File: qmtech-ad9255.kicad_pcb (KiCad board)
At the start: 4 copper layers, 70 x 90 mm, 78 parts

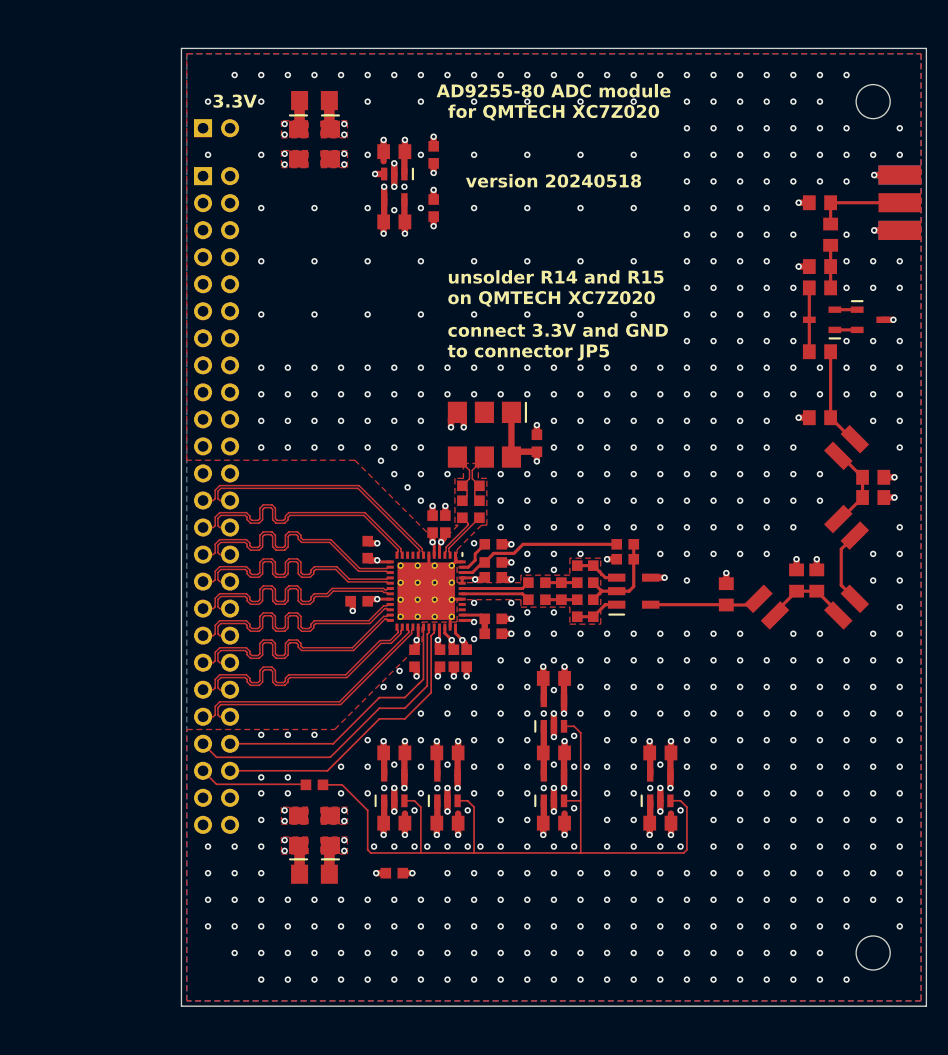
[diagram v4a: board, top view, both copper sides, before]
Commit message: replace TPS7A20 with TLV1117LV in qmtech-ad9255
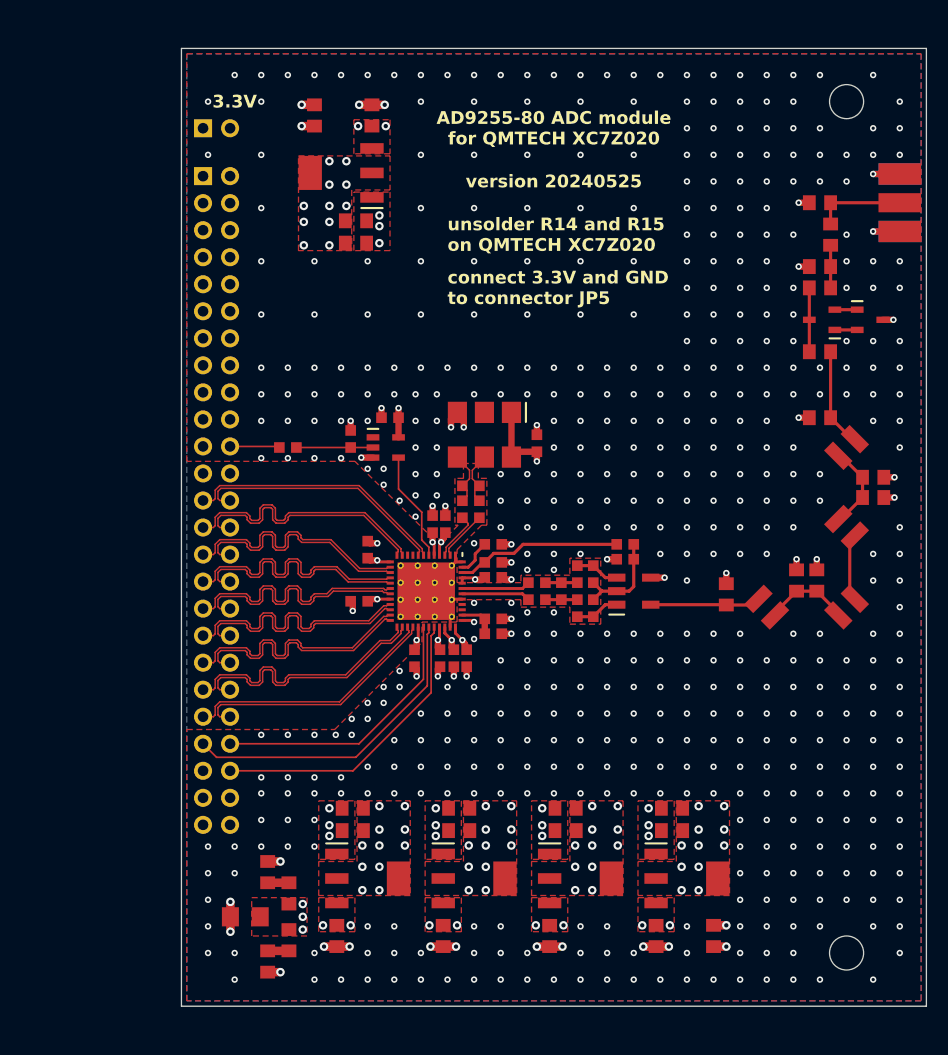
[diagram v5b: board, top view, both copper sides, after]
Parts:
- removed C31, C32: , footprints:CASE-A-3216
- removed FB2: , footprints:1206
- added R14: , footprints:0805, F.Cu at (175.0, 130.9)
- added R15: , footprints:0805, F.Cu at (141.1, 118.9)
- added R16: , footprints:0805, F.Cu at (151.1, 118.9)
- added R17: , footprints:0805, F.Cu at (161.1, 118.9)
- added R18: , footprints:0805, F.Cu at (171.1, 118.9)
- added R19: , footprints:0805, F.Cu at (137.5, 53.8)
- added R20: , footprints:0805, F.Cu at (141.4, 65.8)
- C29: footprint footprints:CASE-A-3216 -> footprints:0805
- C30: footprint footprints:CASE-A-3216 -> footprints:0603
- IC2, IC3, IC4, IC5, IC6: footprint footprints:SOT23-5 -> footprints:SOT223-3
- R12, R13: footprint footprints:0603 -> footprints:0805
- moved R12 72.5 mm to (133.1, 133.3), turned to -90 degrees
- moved C28 68.2 mm to (135.1, 131.3), turned to -90 degrees
- moved C26 55.6 mm to (142.9, 53.8), turned to 90 degrees
- moved IC6 54.6 mm to (140.0, 59.2), turned to 0 degrees
- moved C30 39.2 mm to (144.6, 82.2), turned to 180 degrees
- moved C18 32.2 mm to (139.6, 130.9), turned to -90 degrees
- moved R10 31.8 mm to (135.0, 85.0)
- moved C19 29.8 mm to (141.1, 121.0), turned to 180 degrees
- moved IC2 28.8 mm to (142.5, 125.5), turned to 180 degrees
- moved R11 27.8 mm to (140.9, 84.2), turned to 90 degrees
- moved IC7 24.5 mm to (144.2, 85.0), turned to 180 degrees
- moved IC4 15.1 mm to (162.5, 125.5), turned to 180 degrees
- moved IC5 15.1 mm to (172.5, 125.5), turned to 180 degrees
- moved C22 14.3 mm to (159.6, 130.9), turned to -90 degrees
- moved C24 14.3 mm to (169.6, 130.9), turned to -90 degrees
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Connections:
- C19 pad 1: CVDD -> DVDD
- C21 pad 1: DVDD -> SVDD
- C23 pad 1: SVDD -> AVDD
- C25 pad 1: 3V -> CVDD
- C26 pad 1: AVDD -> VIN2
- C27 pad 1: VCCO33 -> VCCO25
- C28 pad 1: VCCO25 -> 5V
- C28 pad 2: GND -> DMP1
- C29 pad 1: VIN1 -> 5V
- C29 pad 2: GND -> DMP2
- C30 pad 1: 5V -> DVDD
- CN2 pad 22: (no net) -> IN1
- CN2 pad 45: IN1 -> (no net)
- IC1 pad 6: GND -> OE2
- IC2 pad 1: 5V -> GND
- IC2 pad 2: GND -> DVDD
- IC2 pad 3: AEN -> 5V
- IC3 pad 1: 5V -> GND
- IC3 pad 2: GND -> SVDD
- IC3 pad 3: AEN -> 5V
- IC4 pad 1: 5V -> GND
- IC4 pad 2: GND -> AVDD
- IC4 pad 3: AEN -> 5V
- IC5 pad 1: 5V -> GND
- IC5 pad 2: GND -> CVDD
- IC5 pad 3: AEN -> 5V
- IC6 pad 1: 3V -> GND
- IC6 pad 2: GND -> VCCO25
- IC6 pad 3: AEN -> VIN2
- IC7 pad 1: VCCO33 -> (no net)
- IC7 pad 2: GND -> OE1
- IC7 pad 3: VCCO33 -> GND
- IC7 pad 4: GND -> OE2
- IC7 pad 5: VCCO25 -> DVDD
- R10 pad 2: AEN -> OE1
- R11 pad 1: VCCO33 -> OE1
- R12 pad 1: VCCO25 -> DMP1
- R13 pad 1: 5V -> DMP2
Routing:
- net AEN: track 71.8 -> 0.00 mm
- net GND: track 97.4 -> 62.3 mm, vias 658 -> 585
- net 5V: track 16.5 -> 1.20 mm, vias 7 -> 12
- net OE2: track 0.00 -> 10.4 mm
- net VCCO33: track 7.71 -> 0.00 mm, vias 5 -> 0
- net OE1: track 0.00 -> 7.20 mm
- net IN1: track 10.2 -> 4.67 mm
- net 3V: track 4.64 -> 0.00 mm
- net VCCO25: track 4.12 -> 0.00 mm, vias 2 -> 11
- net SVDD: track 5.57 -> 2.35 mm, vias 2 -> 12
- net CVDD: track 10.9 -> 7.70 mm, vias 2 -> 12
- net AVDD: track 15.7 -> 12.4 mm, vias 6 -> 16
- net DMP2: track 0.00 -> 2.00 mm
- net DMP1: track 0.00 -> 2.00 mm
- net VIN2: track 2.74 -> 1.20 mm, vias 2 -> 3
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- added copper zone on F.Cu, net AVDD
- added copper zone on F.Cu, net CVDD
- added copper zone on F.Cu, net DVDD
- added copper zone on F.Cu, net SVDD
- added copper zone on F.Cu, net VCCO25
- removed copper zone on F.Cu, net VCCO33
- removed copper zone on In2.Cu, net VCCO33
- removed copper zone on F.Cu, net VIN1
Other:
- board text added: "version 20240525"
- board text removed: "version 20240518"

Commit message: improve mounting hole positions in qmtech-ad9255
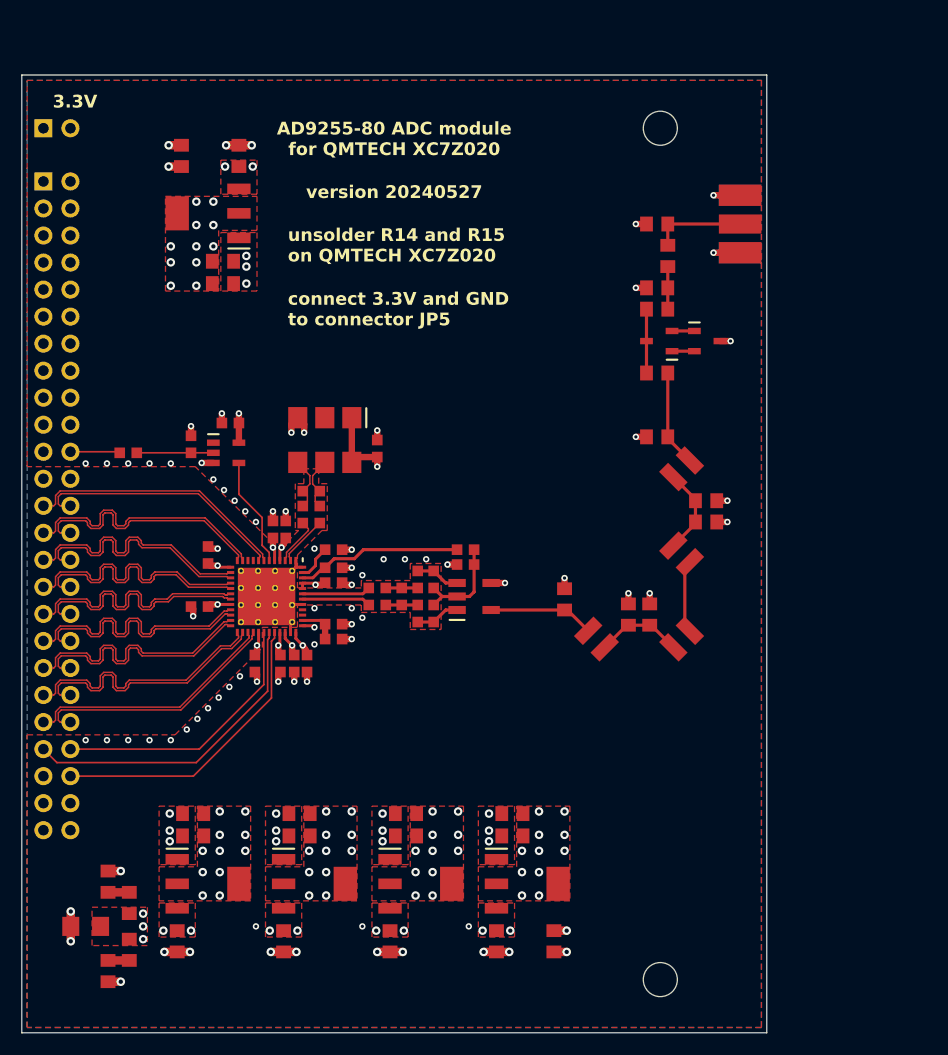
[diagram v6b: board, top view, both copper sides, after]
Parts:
- moved H1 17.7 mm to (170.0, 135.0)
- moved H2 17.7 mm to (170.0, 55.0)
- moved L4 16.3 mm to (164.0, 103.0)
- moved C39 16.1 mm to (167.0, 100.7)
- moved C38 16.0 mm to (169.0, 100.7)
- moved C37 15.9 mm to (174.3, 92.0)
- moved C36 15.9 mm to (174.3, 90.0)
- moved L3 15.8 mm to (172.0, 103.0)
- moved L2 15.7 mm to (172.0, 95.0)
- moved L1 15.6 mm to (172.0, 87.0)
- moved C33 15.4 mm to (169.7, 72.0)
- moved C34 15.4 mm to (169.7, 78.0)
- moved R21 15.4 mm to (170.7, 67.0)
- moved R22 15.4 mm to (169.7, 64.0)
- moved R23 15.4 mm to (169.7, 70.0)
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- renumbered R14 to R21, R15 to R22, R16 to R23
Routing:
- net FLT3: track 6.34 -> 6.84 mm
- net GND: vias 585 -> 95
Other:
- board text added: "version 20240527"
- board text removed: "version 20240525"

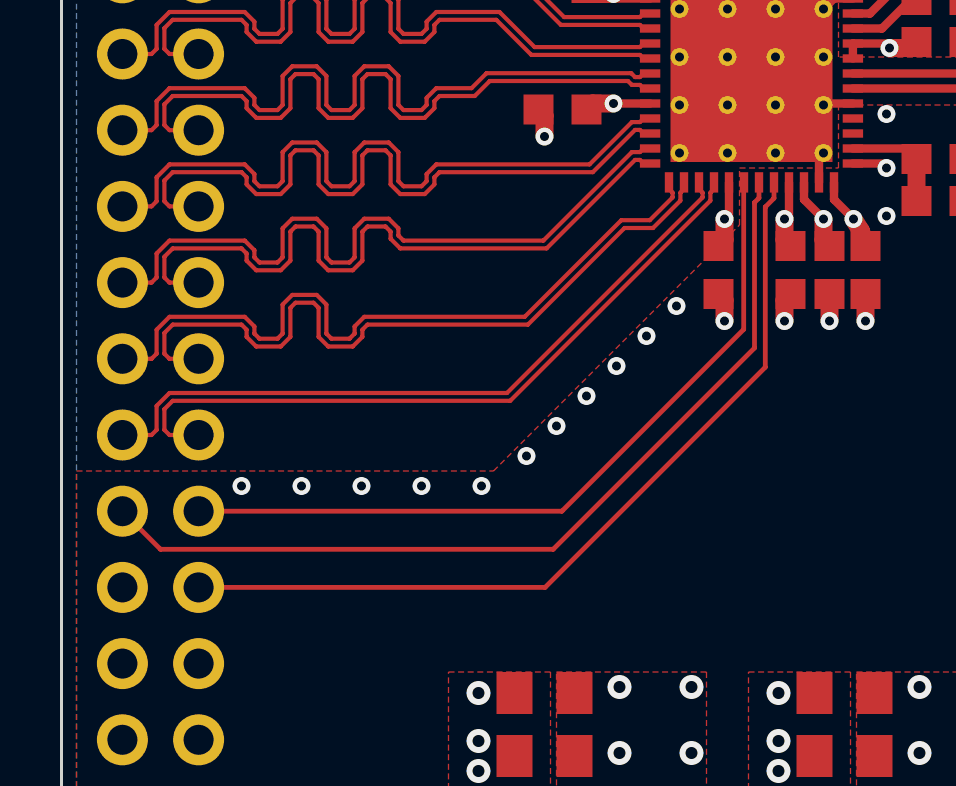
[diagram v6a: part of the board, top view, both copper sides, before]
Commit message: add resistors to SPI inputs in qmtech-ad9255
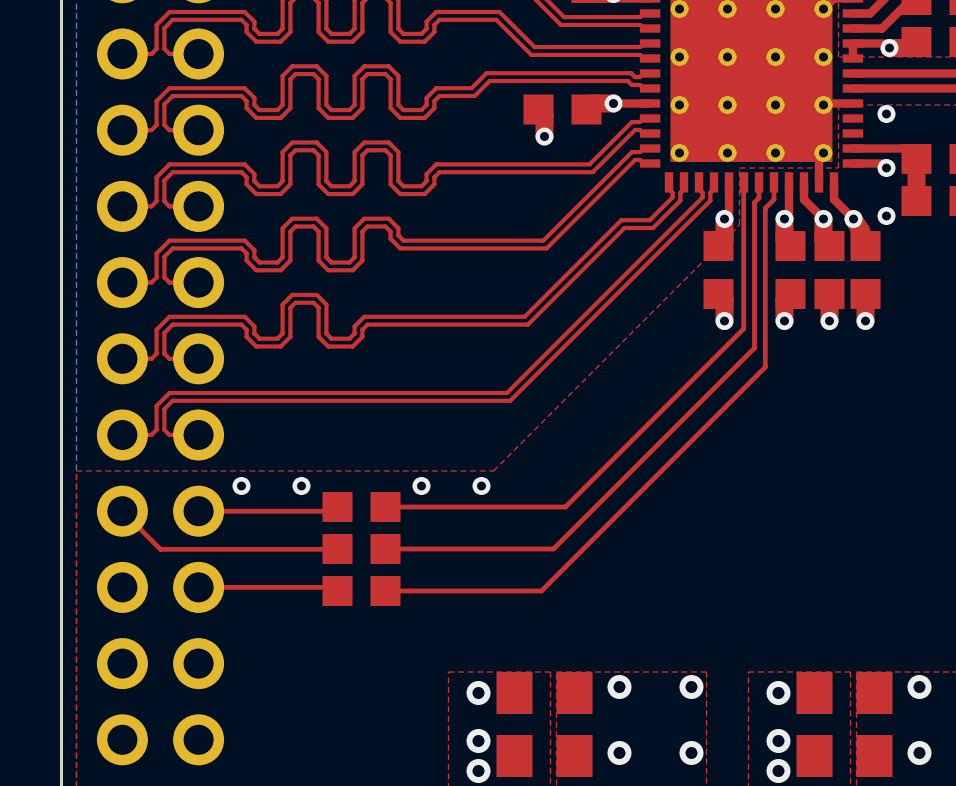
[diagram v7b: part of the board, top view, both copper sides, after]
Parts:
- added R12: , footprints:0603, F.Cu at (120.0, 116.0)
- added R13: , footprints:0603, F.Cu at (120.0, 114.6)
- added R14: , footprints:0603, F.Cu at (120.0, 113.2)
- renumbered R12 to R15, R13 to R16, R14 to R17, R15 to R18, R16 to R19, R17 to R20, R18 to R21, R19 to R22, R20 to R23, R21 to R24, R22 to R25, R23 to R26
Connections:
- CN2 pad 43: SCLK -> SCLK1
- CN2 pad 44: SDIO -> SDIO1
- CN2 pad 46: CSB -> CSB1
- IC1 pad 30: SDIO -> SDIO2
- IC1 pad 31: SCLK -> SCLK2
- IC1 pad 32: CSB -> CSB2
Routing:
- net SCLK: track 30.0 -> 0.00 mm
- net CSB: track 28.2 -> 0.00 mm
- net SDIO: track 25.6 -> 0.00 mm
- net CSB2: track 0.00 -> 22.0 mm
- net SCLK2: track 0.00 -> 20.7 mm
- net SDIO2: track 0.00 -> 19.3 mm
- net SCLK1: track 0.00 -> 7.70 mm
- net SDIO1: track 0.00 -> 4.69 mm
- net CSB1: track 0.00 -> 4.68 mm
- net GND: vias 95 -> 88

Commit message: rename IN1 to OEB1 in qmtech-ad9255
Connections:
- net IN1 renamed OEB1
- net OE1 renamed OEB2
- net OE2 renamed OEB3
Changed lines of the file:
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@@
   (net 37 "5V")
   (net 38 "VCCO25")
-  (net 39 "IN1")
+  (net 39 "OEB2")
   (net 40 "VCM2")
   (net 41 "CSB2")
@@
   (net 56 "DMP1")
   (net 57 "DMP2")
-  (net 58 "OE1")
-  (net 59 "OE2")
+  (net 58 "OEB3")
+  (net 59 "OEB1")
   (net 60 "SCLK1")
   (net 61 "SDIO1")
@@
     )
     (pad "1" smd rect (at -0.8 0 90) (size 1 1) (layers "F.Cu" "F.Paste" "F.Mask")
-      (net 58 "OE1"))
+      (net 39 "OEB2"))
     (pad "2" smd rect (at 0.8 0 90) (size 1 1) (layers "F.Cu" "F.Paste" "F.Mask")
       (net 3 "GND"))
@@
     (pad "1" smd rect (at 1.2 0.95 270) (size 0.6 1.2) (layers "F.Cu" "F.Paste" "F.Mask"))
     (pad "2" smd rect (at 1.2 0 270) (size 0.6 1.2) (layers "F.Cu" "F.Paste" "F.Mask")
-      (net 58 "OE1"))
+      (net 39 "OEB2"))
     (pad "3" smd rect (at 1.2 -0.95 270) (size 0.6 1.2) (layers "F.Cu" "F.Paste" "F.Mask")
       (net 3 "GND"))
     (pad "4" smd rect (at -1.2 -0.95 270) (size 0.6 1.2) (layers "F.Cu" "F.Paste" "F.Mask")
-      (net 59 "OE2"))
+      (net 58 "OEB3"))
     (pad "5" smd rect (at -1.2 0.95 270) (size 0.6 1.2) (layers "F.Cu" "F.Paste" "F.Mask")
       (net 2 "DVDD"))
@@
       (net 1 "AVDD"))
     (pad "6" smd rect (at -3.38 -0.25 270) (size 0.68 0.28) (layers "F.Cu" "F.Paste" "F.Mask")
-      (net 59 "OE2"))
+      (net 58 "OEB3"))
     (pad "7" smd rect (at -3.38 0.25 270) (size 0.68 0.28) (layers "F.Cu" "F.Paste" "F.Mask")
       (net 13 "DCON"))
@@
     )
     (pad "1" smd rect (at -0.8 0) (size 1 1) (layers "F.Cu" "F.Paste" "F.Mask")
-      (net 39 "IN1"))
+      (net 59 "OEB1"))
     (pad "2" smd rect (at 0.8 0) (size 1 1) (layers "F.Cu" "F.Paste" "F.Mask")
-      (net 58 "OE1"))
+      (net 39 "OEB2"))
   )
   (footprint "footprints:0603" (layer "F.Cu")
@@
     (pad "21" thru_hole circle (at -25.4 -1.27 90) (size 1.7 1.7) (drill 1) (layers "*.Cu" "*.Mask") (remove_unused_layers) (keep_end_layers) (zone_layer_connections))
     (pad "22" thru_hole circle (at -25.4 1.27 90) (size 1.7 1.7) (drill 1) (layers "*.Cu" "*.Mask") (remove_unused_layers) (keep_end_layers) (zone_layer_connections)
-      (net 39 "IN1"))
+      (net 59 "OEB1"))
     (pad "23" thru_hole circle (at -27.94 -1.27 90) (size 1.7 1.7) (drill 1) (layers "*.Cu" "*.Mask") (remove_unused_layers) (keep_end_layers) (zone_layer_connections))
     (pad "24" thru_hole circle (at -27.94 1.27 90) (size 1.7 1.7) (drill 1) (layers "*.Cu" "*.Mask") (remove_unused_layers) (keep_end_layers) (zone_layer_connections))
@@
   (via (at 126.4 67.6) (size 0.8) (drill 0.4) (layers "F.Cu" "B.Cu") (remove_unused_layers) (keep_end_layers) (free) (zone_layer_connections "In2.Cu") (net 38))
   (via (at 126.4 61.9) (size 0.8) (drill 0.4) (layers "F.Cu" "B.Cu") (remove_unused_layers) (keep_end_layers) (free) (zone_layer_connections "In2.Cu") (net 38))
-  (segment (start 114.57 85.4) (end 119.1 85.4) (width 0.16) (layer "F.Cu") (net 39))
-  (segment (start 119.1 85.4) (end 119.2 85.5) (width 0.16) (layer "F.Cu") (net 39))
+  (segment (start 125.9 85.5) (end 128 85.5) (width 0.16) (layer "F.Cu") (net 39))
+  (segment (start 120.8 85.5) (end 125.9 85.5) (width 0.16) (layer "F.Cu") (net 39))
   (segment (start 152.5 96) (end 152.5 94.6) (width 0.3) (layer "F.Cu") (net 40))
   (segment (start 149.5 99) (end 148.7 99.8) (width 0.3) (layer "F.Cu") (net 40))
@@
   (segment (start 120.1 133.2) (end 118.1 133.2) (width 0.8) (layer "F.Cu") (net 56))
   (segment (start 120.1 126.8) (end 118.1 126.8) (width 0.8) (layer "F.Cu") (net 57))
-  (segment (start 125.9 85.5) (end 128 85.5) (width 0.16) (layer "F.Cu") (net 58))
-  (segment (start 120.8 85.5) (end 125.9 85.5) (width 0.16) (layer "F.Cu") (net 58))
-  (segment (start 130.4 89.4) (end 132.58 91.58) (width 0.16) (layer "F.Cu") (net 59))
-  (segment (start 132.58 94.200244) (end 133.25 94.870244) (width 0.16) (layer "F.Cu") (net 59))
-  (segment (start 132.58 91.58) (end 132.58 94.200244) (width 0.16) (layer "F.Cu") (net 59))
-  (segment (start 133.25 94.870244) (end 133.25 95.62) (width 0.16) (layer "F.Cu") (net 59))
-  (segment (start 130.4 86.45) (end 130.4 89.4) (width 0.16) (layer "F.Cu") (net 59))
+  (segment (start 130.4 89.4) (end 132.58 91.58) (width 0.16) (layer "F.Cu") (net 58))
+  (segment (start 132.58 94.200244) (end 133.25 94.870244) (width 0.16) (layer "F.Cu") (net 58))
+  (segment (start 132.58 91.58) (end 132.58 94.200244) (width 0.16) (layer "F.Cu") (net 58))
+  (segment (start 133.25 94.870244) (end 133.25 95.62) (width 0.16) (layer "F.Cu") (net 58))
+  (segment (start 130.4 86.45) (end 130.4 89.4) (width 0.16) (layer "F.Cu") (net 58))
+  (segment (start 114.57 85.4) (end 119.1 85.4) (width 0.16) (layer "F.Cu") (net 59))
+  (segment (start 119.1 85.4) (end 119.2 85.5) (width 0.16) (layer "F.Cu") (net 59))
   (segment (start 119.19 114.61) (end 119.2 114.6) (width 0.16) (layer "F.Cu") (net 60))
   (segment (start 113.3 114.61) (end 119.19 114.61) (width 0.16) (layer "F.Cu") (net 60))
